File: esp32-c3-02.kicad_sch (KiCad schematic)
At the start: 5 parts

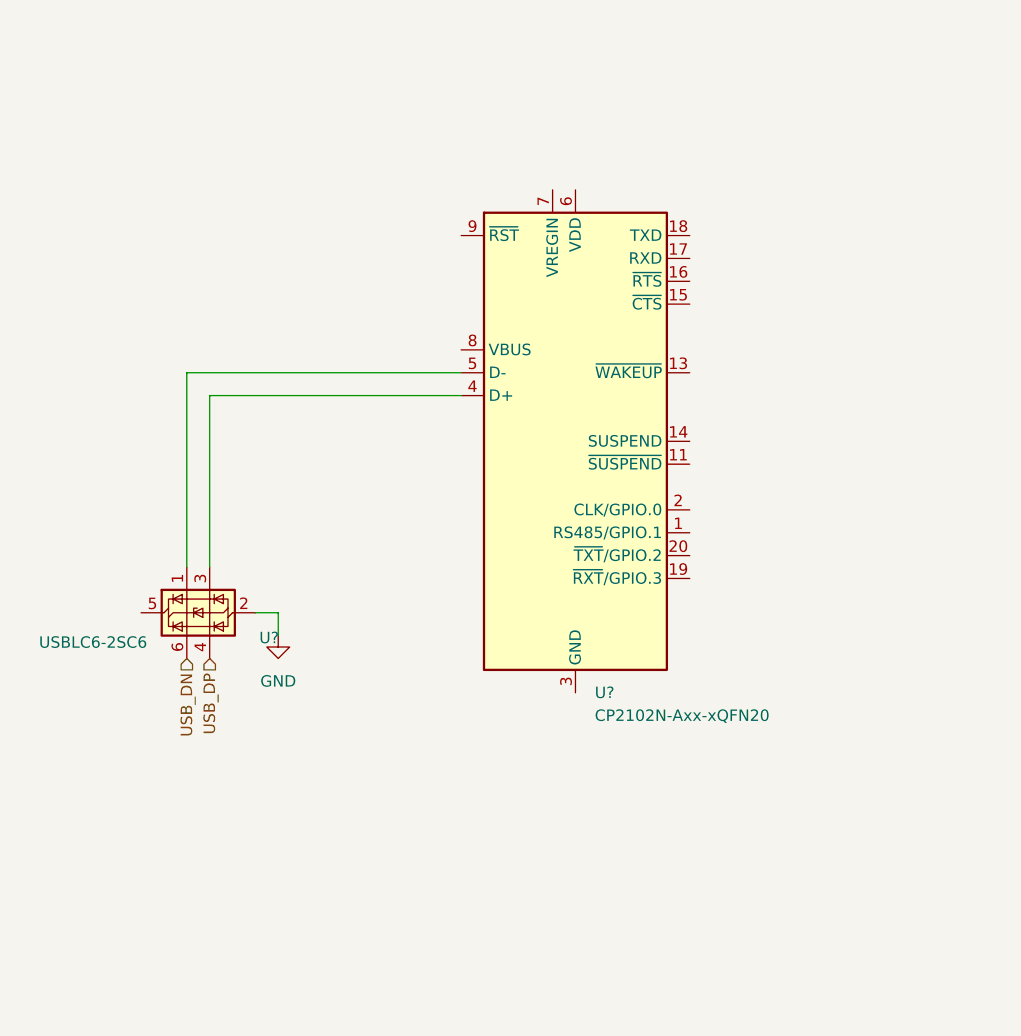
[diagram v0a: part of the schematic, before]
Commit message: Wire USB-to-UART module
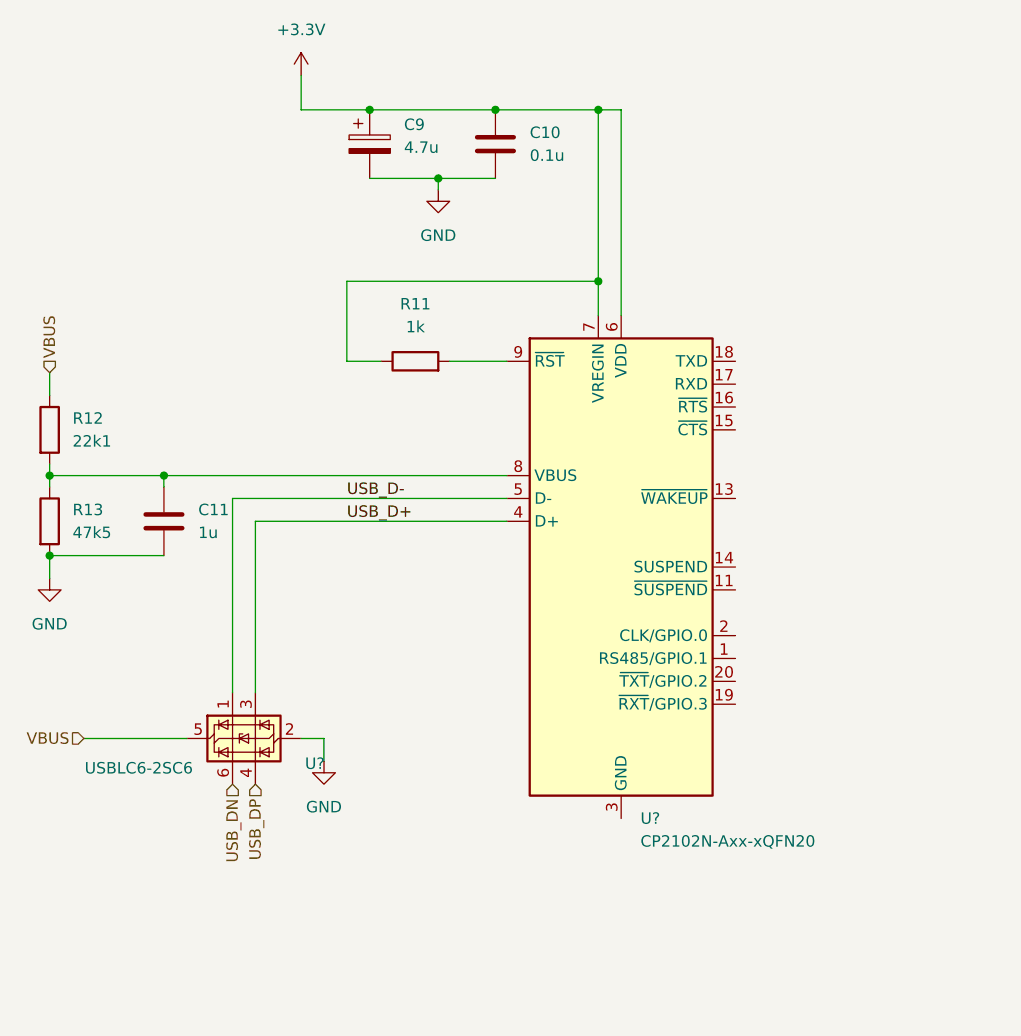
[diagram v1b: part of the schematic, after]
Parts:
- added C10: 0.1u, symbol Device:C
- added C11: 1u, symbol Device:C
- added C9: 4.7u, symbol Device:C_Polarized
- added R11: 1k, symbol Device:R
- added R12: 22k1, symbol Device:R
- added R13: 47k5, symbol Device:R
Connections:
- net GND: now also C10.1, C11.2, C9.2, R13.2
- net USB_D-: now reaches U?.1 (I/O1), U?.5 (D-)
- net USB_D+: now reaches U?.3 (I/O2), U?.4 (D+)
- net VBUS: now reaches U?.5 (VBUS)
- net VBUS: now also R12.1
- net +3.3V: now reaches U?.6 (VDD)
- net +3.3V: now also U?.7 (VREGIN), C10.2, C9.1, R11.1
- net at U?.8 (VBUS): now also C11.1, R12.2, R13.1
- net at U?.9 (~{RST}): now also R11.2
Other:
- moved on the sheet: U?

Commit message: Connect ESP32-C3 peripherals
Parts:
- added C7: 10u, symbol Device:C_Polarized
- added C8: 0.1u, symbol Device:C
- added LED?: LTST-C170GKT, LEDC2012X120N, symbol LTST-C170GKT:LTST-C170GKT
- added LED?: LTST-C170KRKT, LEDC2012X120N, symbol LTST-C170KRKT:LTST-C170KRKT
- added R15, R20: 50, symbol Device:R
- added R? (x2): 470k, symbol Device:R
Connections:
- net +3.3V: now also U?.1 (3V3), C7.1, C8.2, LED?.2 (A), LED?.2 (A)
- net GND: now also U?.19 (GND), U?.20 (GND), U?.21 (GND), U?.22 (GND), U?.23 (GND), U?.24 (GND), U?.25 (GND), U?.26 (GND), U?.27 (GND), U?.28 (GND), U?.29 (GND), U?.30 (GND), U?.31 (GND), U?.32 (GND), U?.33 (GND), U?.34 (GND), U?.35 (GND), U?.36 (GND), U?.37 (GND), U?.38 (GND), U?.39 (GND), U?.9 (GND), C7.2, C8.1
- net CS: now reaches U?.10 (IO10)
- net TX_RX: now reaches U?.11 (RXD)
- net TX_RX: now also U?.18 (TXD)
- net RX_TX: now reaches U?.12 (TXD)
- net RX_TX: now also U?.17 (RXD)
- net GPIO_18: now reaches U?.13 (IO18)
- net GPIO_19: now reaches U?.14 (IO19)
- net SCL: now reaches U?.15 (IO3)
- net MISO_D0: now reaches U?.16 (IO2)
- net PHOTO_C: now reaches U?.17 (IO1)
- net CS_SD: now reaches U?.18 (IO0)
- net EN: now reaches U?.2 (EN)
- net SDA: now reaches U?.3 (IO4)
- net MIC_OUT: now reaches U?.4 (IO5)
- net at U?.5 (IO6): now also R20.1
- net at U?.6 (IO7): now also R15.2
- net GPIO8: now reaches U?.7 (IO8)
- net BOOT: now reaches U?.8 (IO9)
- net DTS: now reaches U?.15 (~{CTS})
- net RTS: now reaches U?.16 (~{RTS})
- net at U?.19 (~{RXT}/GPIO.3): now also R?.1
- net at U?.20 (~{TXT}/GPIO.2): now also R?.1
- new net: LED?.1 (K), R?.2 (x2)
- new net MOSI_DI: R15.1
- new net SCLK: R20.2
- no-connect marks 0 -> 5
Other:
- note added: "ESP32-C3 Module"
- note added: "USB-to-UART Module"
- moved on the sheet: C10, C11, C9, R11, R12, R13, U?
